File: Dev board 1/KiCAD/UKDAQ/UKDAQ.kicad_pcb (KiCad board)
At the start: 2 copper layers, 41 x 24.5 mm, 22 parts, among them J1 5 pin Molex (0537800570), U1 AP2210N_SOT-23-3, U2 PI4ULS5V202, U3 BNO055, U4 BME280, U5 MAX32660-24TQFN-EP, Y1 Crystal

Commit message: oops i forgot to push this for a while
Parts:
- added G***: LOGO, Joseph:LilypadAerospace_3mm, B.Cu at (142.2, 106.7)

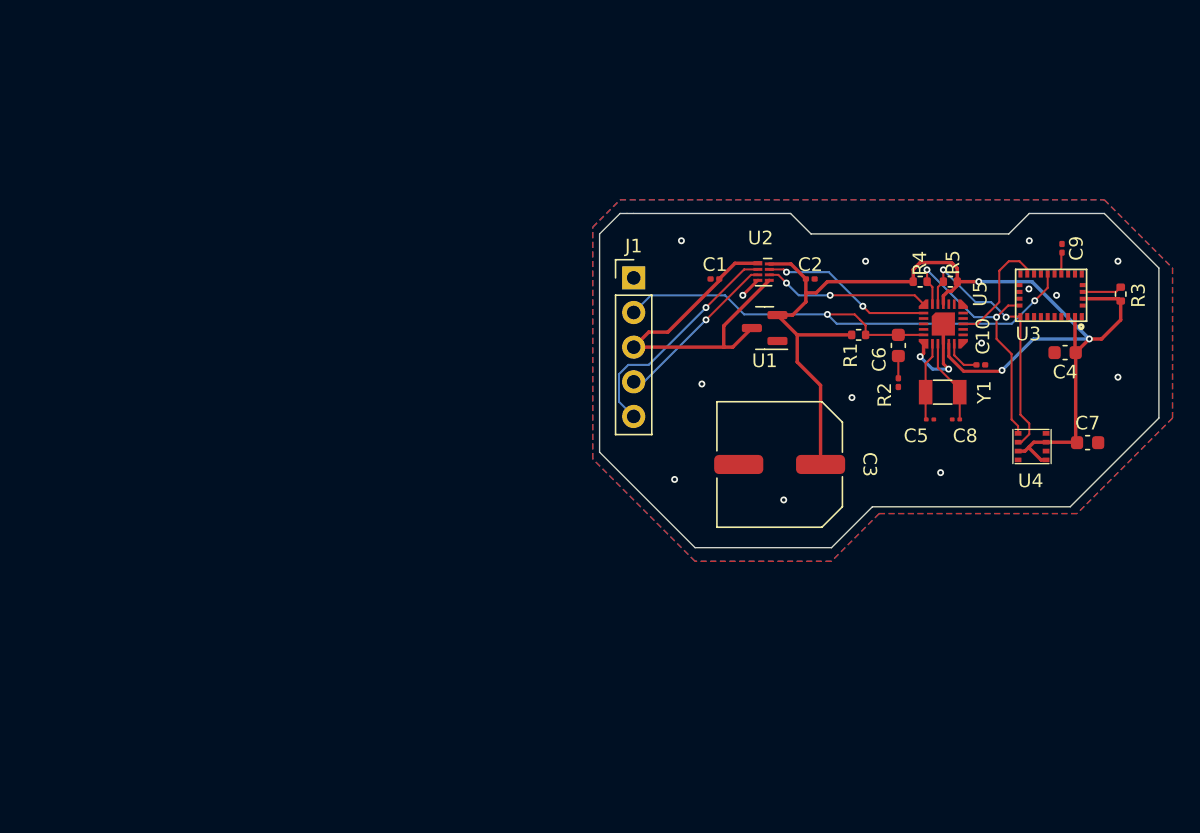
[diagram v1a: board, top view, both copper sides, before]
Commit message: updated dev board 1 to rev 2 design
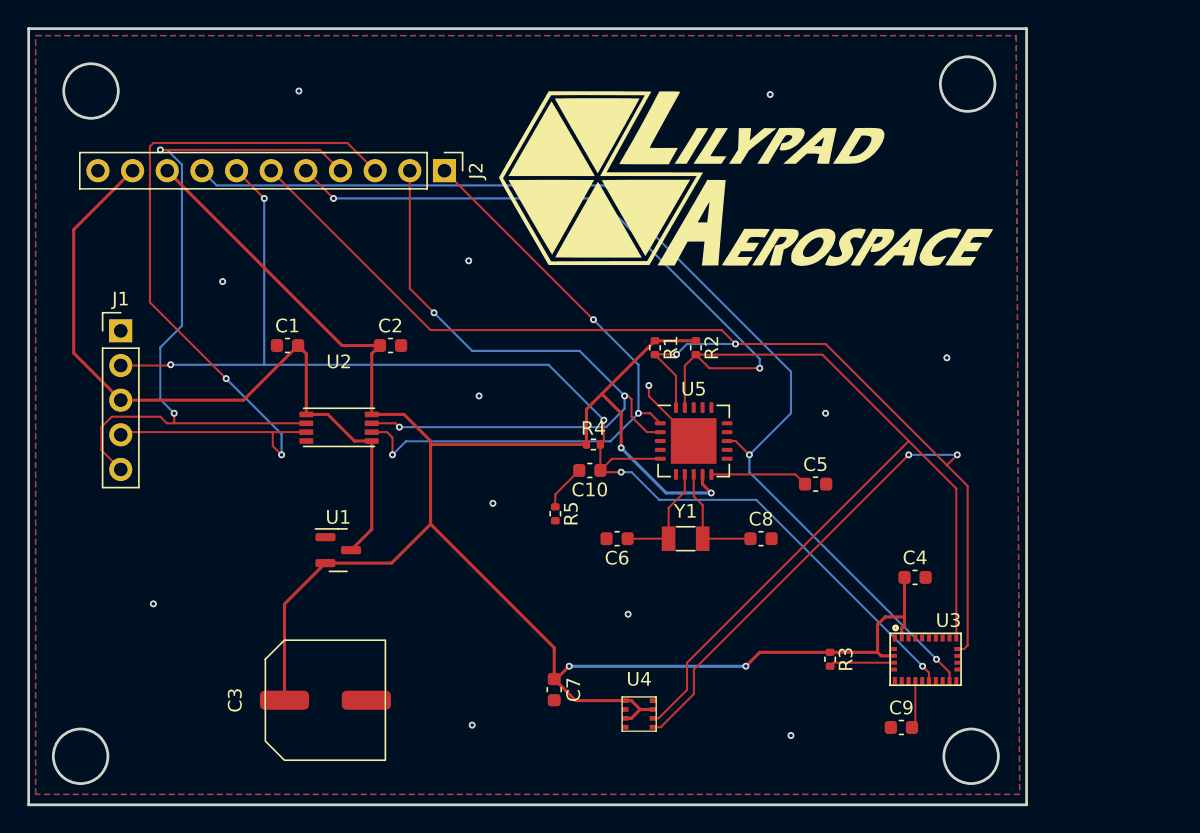
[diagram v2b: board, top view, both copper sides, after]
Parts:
- added J2: Conn_01x11_Male, Connector_PinHeader_2.54mm:PinHeader_1x11_P2.54mm_Vertical, F.Cu at (109.7, 91.2)
- C1, C2, C9: footprint Capacitor_SMD:C_0201_0603Metric -> Capacitor_SMD:C_0603_1608Metric
- C10: value 1 uF -> 100 nF; footprint Capacitor_SMD:C_0201_0603Metric -> Capacitor_SMD:C_0603_1608Metric
- C5: value 6 pF -> 1 uF; footprint Capacitor_SMD:C_01005_0402Metric -> Capacitor_SMD:C_0603_1608Metric
- C6: value 100 nF -> 6 pF
- C8: footprint Capacitor_SMD:C_01005_0402Metric -> Capacitor_SMD:C_0603_1608Metric
- G***: moved to F.Cu
- R1: value 10k -> 4.7k
- R2: value 10 -> 4.7k; footprint Resistor_SMD:R_0201_0603Metric -> Resistor_SMD:R_0402_1005Metric
- R4: value 4.7k -> 10k
- R5: value 4.7k -> 10
- U2: footprint Package_DFN_QFN:OnSemi_UDFN-8_1.2x1.8mm_P0.4mm -> Joseph:MSOP-8
- U5: value MAX32660-24TQFN-EP -> MAX32660-20TQFN-EP; footprint Joseph:MAX32660-24-TQFN-EP -> Package_DFN_QFN:QFN-20-1EP_5x5mm_P0.65mm_EP3.35x3.35mm
- moved C7 43.1 mm to (117.8, 129.2), turned to -90 degrees
- moved J1 37.8 mm to (86.0, 102.9)
- moved C3 37.5 mm to (101.0, 130.0), turned to 90 degrees
- moved C9 37.0 mm to (143.2, 132.0), turned to 0 degrees
- moved U1 35.2 mm to (101.9, 119.0), turned to 0 degrees
- moved U4 34.8 mm to (124.0, 131.0), turned to 0 degrees
- moved R3 34.2 mm to (138.0, 127.0), turned to -90 degrees
- moved R5 33.6 mm to (117.9, 116.3), turned to -90 degrees
- moved U2 33.1 mm to (102.0, 110.0)
- moved C1 31.7 mm to (98.2, 104.0)
- moved C2 31.2 mm to (105.8, 104.0)
- moved C10 29.7 mm to (120.4, 113.2), turned to 180 degrees
- moved U3 28.2 mm to (145.0, 127.0), turned to 0 degrees
- moved R4 26.8 mm to (120.6, 111.3)
- moved C6 25.0 mm to (122.4, 118.2), turned to 180 degrees
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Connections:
- C10 pad 1: Net-(C10-Pad1) -> /nRESET
- C10 pad 2: GND -> Net-(C10-Pad2)
- C6 pad 1: /nRESET -> Net-(C6-Pad1)
- C6 pad 2: Net-(C6-Pad2) -> GND
- R1 pad 2: /nRESET -> /SCL
- R2 pad 1: Net-(C6-Pad2) -> VDD
- R2 pad 2: GND -> /SDA
- R4 pad 2: /SCL -> /nRESET
- R5 pad 1: VDD -> Net-(C10-Pad2)
- R5 pad 2: /SDA -> GND
- U5 pad 10: GND -> Net-(C5-Pad1)
- U5 pad 11: VDD -> unconnected-(U5-Pad11)
- U5 pad 12: Net-(C10-Pad1) -> unconnected-(U5-Pad12)
- U5 pad 13: unconnected-(U5-Pad13) -> /BNO_INTERRUPT
- U5 pad 15: (no net) -> unconnected-(U5-Pad15)
- U5 pad 16: /BNO_INTERRUPT -> unconnected-(U5-Pad16)
- U5 pad 19: unconnected-(U5-Pad19) -> /SDA
- U5 pad 20: unconnected-(U5-Pad20) -> /SCL
- U5 pad 21: unconnected-(U5-Pad21) -> GND
- U5 pad 3: (no net) -> unconnected-(U5-Pad3)
- U5 pad 5: unconnected-(U5-Pad5) -> /nRESET
- U5 pad 6: /nRESET -> GND
- U5 pad 7: GND -> Net-(C6-Pad1)
- U5 pad 8: Net-(C5-Pad1) -> Net-(C8-Pad1)
- U5 pad 9: Net-(C8-Pad1) -> VDD
- Y1 pad 2: Net-(C5-Pad1) -> Net-(C6-Pad1)
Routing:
- net /SCL: track 20.4 -> 116.6 mm, vias 2 -> 4
- net /SDA: track 19.7 -> 111.4 mm
- net /BNO_INTERRUPT: track 8.56 -> 81.3 mm, vias 0 -> 2
- net VDD: track 87.7 -> 155.1 mm, vias 3 -> 4
- net /nRESET: track 41.9 -> 91.5 mm, vias 2 -> 5
- net /RX/SWCLK-VCC: track 12.3 -> 59.7 mm, vias 1 -> 2
- net /TX/SWDIO-VDD: track 12.6 -> 52.3 mm, vias 2 -> 3
- net /TX/SWDIO-VCC: track 16.9 -> 55.1 mm, vias 1 -> 2
- net /RX/SWCLK-VDD: track 12.2 -> 47.8 mm, vias 2 -> 3
- net VCC: track 27.2 -> 54.2 mm
- net Net-(C6-Pad1): track 0.00 -> 8.20 mm
- net Net-(C10-Pad2): track 0.00 -> 3.39 mm
- net GND: track 8.55 -> 5.43 mm, vias 16 -> 13
- net Net-(C10-Pad1): track 2.76 -> 0.00 mm
- net Net-(C8-Pad1): track 6.21 -> 8.48 mm
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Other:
- board size 41 x 24.5 mm -> 73.2 x 56.9 mm

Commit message: changes to board design and new BOM
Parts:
- U5: footprint Package_DFN_QFN:QFN-20-1EP_5x5mm_P0.65mm_EP3.35x3.35mm -> Joseph:21-0139V_T2044&plus_5_MXM
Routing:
- net GND: track 5.43 -> 7.81 mm
- net /SCL: track 116.6 -> 117.2 mm
- net /nRESET: track 91.5 -> 92.1 mm
- net /RX/SWCLK-VDD: track 47.8 -> 48.4 mm
- net /TX/SWDIO-VDD: track 52.3 -> 52.8 mm
- net Net-(C6-Pad1): track 8.20 -> 8.75 mm
- net VDD: track 155.1 -> 155.6 mm
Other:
- board text added: "LA-UKDAQ-rev_0.5-6/21/23"
- board text added: "Orient text this way"
